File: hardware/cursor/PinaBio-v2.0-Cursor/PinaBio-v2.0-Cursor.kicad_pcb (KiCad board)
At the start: 4 copper layers, 81.3 x 57.2 mm, 80 parts, among them J1 USB-C, J2 J_BATT, J3 J_ECG, J4 J_PPG, J5 J_TEMP, J6 J_GSR, J7 J_RESP_T, J8 J_RESP_A, Q1 BSS84, Q2 BSS138, Q3 BSS138, SW1 SW_DPDT, SW2 BOOT, U1 USBLC6-2SC6, U2 BQ24074, U3 TPS63070, U4 TLV75530PDBVR, U5 ESP32-S3-MINI-1U-N8, U6 ADS122C04, U7 ADS122C04, U8 MCP6004

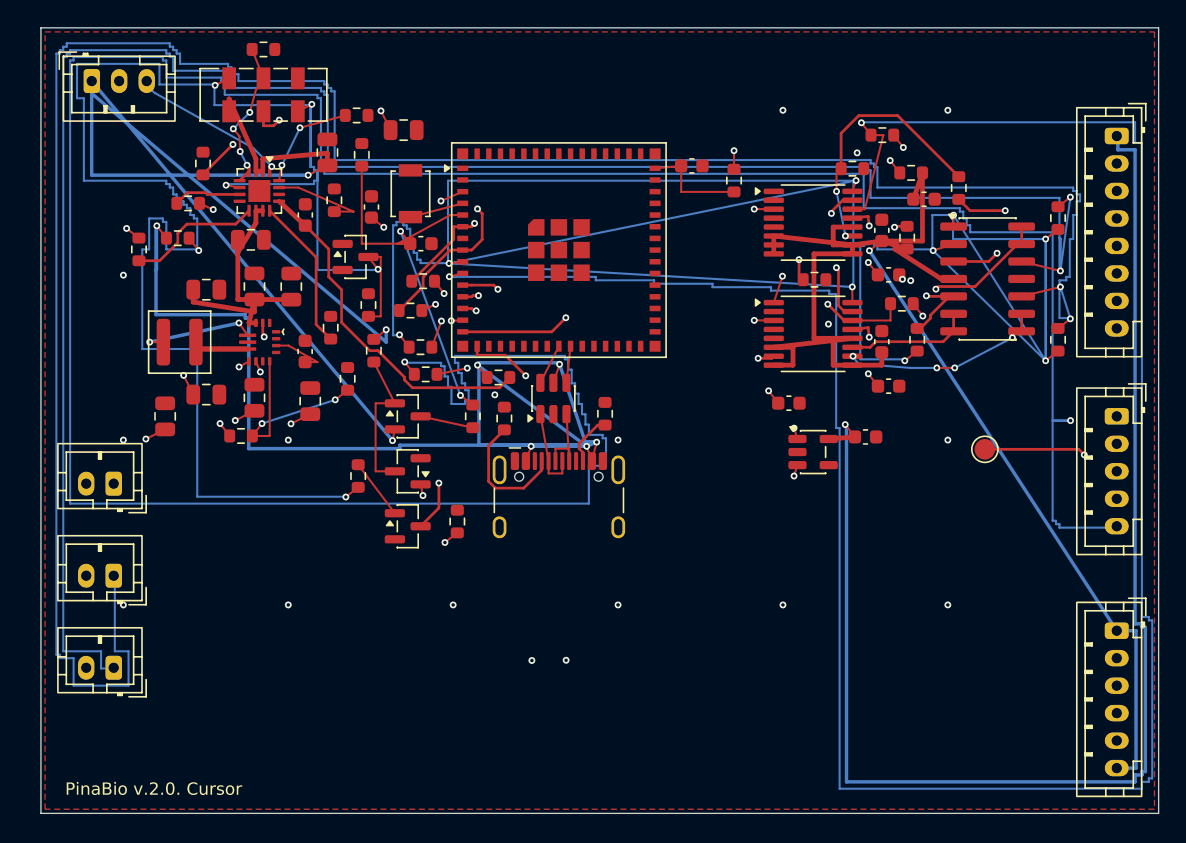
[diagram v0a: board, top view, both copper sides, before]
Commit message: Update the Cursor KiCad board to SPEC-0.9
Place the ESP32-S3-MINI-1U U.FL end on the board edge with a copper
keepout, split digital and analogue ground through one wide net tie, and
keep the six electrical changes. ERC and DRC are clean and the fab outputs
are regenerated.
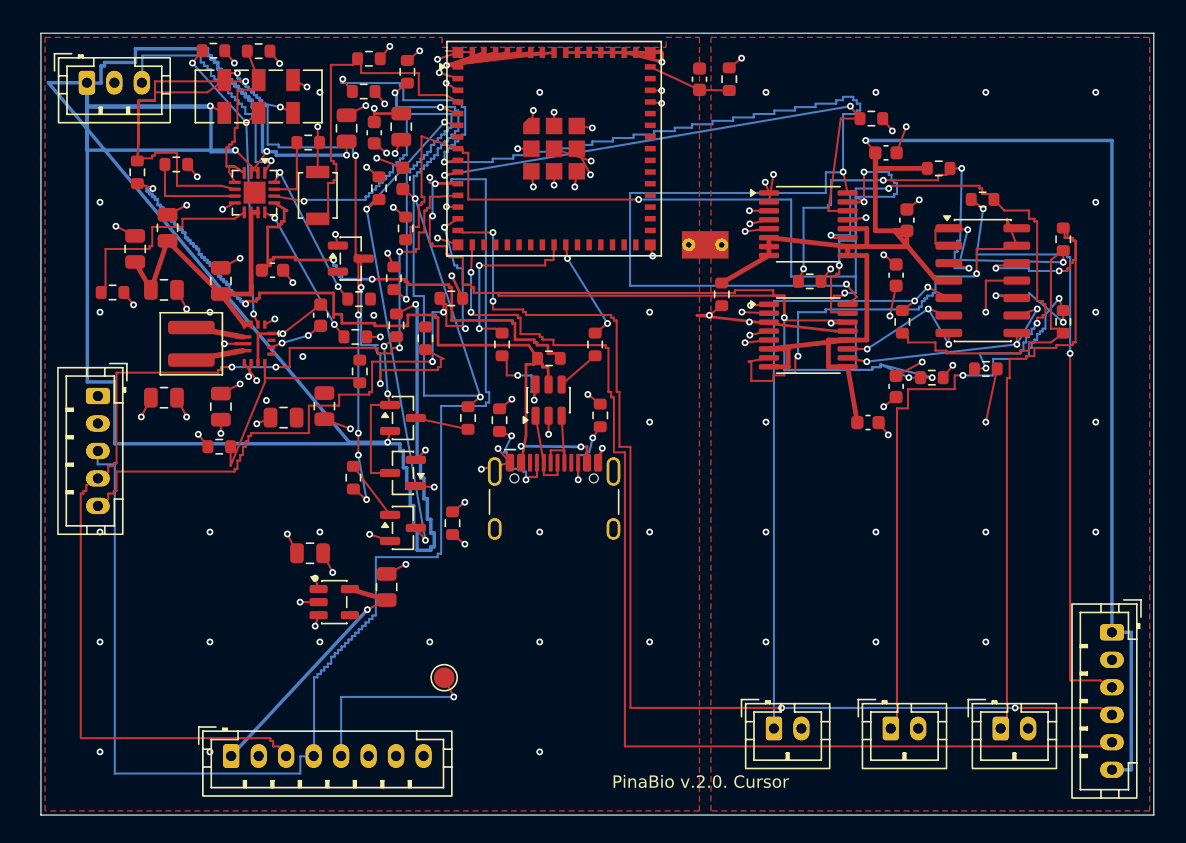
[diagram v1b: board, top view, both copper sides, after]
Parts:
- added NT1: GND_TIE, GndTie_2mm, F.Cu at (48.3, 15.8)
- added R35: 22, R_0603_1608Metric, F.Cu at (33.6, 23.0)
- added R36: 22, R_0603_1608Metric, F.Cu at (40.3, 23.0)
- added R37: 46.4k 1%, R_0603_1608Metric, F.Cu at (25.7, 18.2)
- added R38: 10k, R_0603_1608Metric, F.Cu at (23.9, 2.25)
- C12, C13: footprint C_0603_1608Metric -> C_0805_2012Metric
- moved J5 78.7 mm to (13.8, 53.0), turned to 0 degrees
- moved J4 74.2 mm to (4.14, 26.8)
- moved J8 64.7 mm to (69.8, 51.0), turned to 0 degrees
- moved J7 57.6 mm to (61.8, 51.0), turned to 0 degrees
- moved J6 51.2 mm to (53.3, 51.0), turned to 0 degrees
- moved TP1 42.7 mm to (29.3, 47.3)
- moved U4 36.5 mm to (21.3, 41.8)
- moved C13 36.5 mm to (25.2, 40.7), turned to 90 degrees
- moved C12 36.5 mm to (19.6, 38.2)
- moved R24 19.1 mm to (23.5, 4.63)
- moved R34 17.5 mm to (68.8, 24.8)
- moved R15 16.4 mm to (49.5, 19.4), turned to 90 degrees
- moved R6 13.4 mm to (23.2, 19.7)
- moved C5 9.27 mm to (8.95, 19.1), turned to 0 degrees
- moved R12 8.25 mm to (12.6, 1.66), turned to 0 degrees
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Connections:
- C18 pad 2: /GND -> /AGND
- C19 pad 2: /GND -> /AGND
- C20 pad 2: /GND -> /AGND
- C21 pad 2: /GND -> /AGND
- C22 pad 2: /GND -> /AGND
- J3 pad 2: /GND -> /AGND
- J6 pad 2: /GND -> /AGND
- J7 pad 2: /GND -> /AGND
- J8 pad 2: /GND -> /AGND
- R29 pad 2: /GND -> /AGND
- R34 pad 2: /GND -> /AGND
- U2 pad 14: (no net) -> /TMR
- U5 pad 23: /USB_DM -> /USB_DM_IO
- U5 pad 24: /USB_DP -> /USB_DP_IO
- U6 pad 1: /GND -> /AGND
- U6 pad 2: /GND -> /AGND
- U6 pad 4: /GND -> /AGND
- U6 pad 5: /GND -> /AGND
- U7 pad 2: /GND -> /AGND
- U7 pad 4: /GND -> /AGND
- U7 pad 5: /GND -> /AGND
- U8 pad 11: /GND -> /AGND
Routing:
- net /PPG_INT: track 233.4 -> 53.3 mm, vias 3 -> 4
- net /GND: track 0.00 -> 152.8 mm, vias 16 -> 75
- net /DRDY_ECG: track 168.2 -> 41.7 mm
- net /SNS_TH: track 164.4 -> 51.8 mm, vias 2 -> 4
- net /SNS_AB: track 149.6 -> 54.0 mm
- net /BAT_PROT: track 103.7 -> 198.2 mm, vias 3 -> 6
- net /3V0_TEMP: track 100.4 -> 18.9 mm
- net /DRDY_SLOW: track 33.4 -> 99.2 mm, vias 2 -> 7
- net /VLOG: track 157.4 -> 101.7 mm, vias 6 -> 10
- net /0V5_EXC: track 87.7 -> 36.2 mm, vias 5 -> 2
- net /SDA_ADC: track 47.2 -> 85.2 mm, vias 3 -> 5
- net /VBUS: track 99.9 -> 62.4 mm, vias 6 -> 4
- net /TMR: track 0.00 -> 37.1 mm, vias 0 -> 2
- net /AGND: track 0.00 -> 28.4 mm, vias 0 -> 30
- net /BAT_SENSE: track 30.3 -> 58.7 mm, vias 2 -> 4
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- added copper zone on F.Cu, net /AGND
- added copper zone on In1.Cu, net /AGND
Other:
- board size 81.3 x 57.2 mm -> 81 x 56.9 mm

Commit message: Add connector labels, the PINA logo and the Paca name on the Cursor board silk.
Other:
- board text added: "3V0"
- board text added: "3V3"
- board text added: "AB"
- board text added: "AGND"
- board text added: "BAT+"
- board text added: "BATERIA"
- board text added: "CC1"
- board text added: "CC2"
- board text added: "D+"
- board text added: "D-"
- board text added: "ECG"
- board text added: "GND"
- board text added: "GSR"
- board text added: "INT"
- board text added: "LO+"
- board text added: "LO-"
- board text added: "OS"
- board text added: "OUT"
- board text added: "PPG"
- board text added: "PinaBio "Paca" v2.0"
- board text added: "RESP A"
- board text added: "RESP T"
- board text added: "SBU"
- board text added: "SCL"
- board text added: "SDA"
- board text added: "TEMP"
- board text added: "TH"
- board text added: "TS"
- board text added: "USB"
- board text added: "VBUS"
- board text removed: "PinaBio v.2.0. Cursor"

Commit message: Fix mirrored TPS63070 footprint (TI 4222000/B), reroute the TPS63070 zone, portable library tables
U3 pin 1 is now top left with counter-clockwise numbering, pads 9-11 use the TI sizes, L1 sits east of U3 with both switch nodes on F.Cu without vias. fp-lib-table and sym-lib-table use KIPRJMOD and KICAD9_SYMBOL_DIR. ERC, DRC, fab, position, netlist and render regenerated.
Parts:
- moved R14 11.1 mm to (12.1, 24.9), turned to 180 degrees
- moved L1 8.86 mm to (19.8, 23.3)
- moved C11 8.58 mm to (12.1, 23.2), turned to 180 degrees
- moved R8 8.03 mm to (18.3, 15.9)
- moved R13 3.94 mm to (15.0, 27.1), turned to 90 degrees
- turned U3 to 0 degrees
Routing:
- net /FB: track 17.5 -> 2.54 mm
- net /ILIM: track 10.9 -> 2.14 mm
- net /GND: track 152.8 -> 147.4 mm, vias 75 -> 84
- net /VAUX: track 3.96 -> 0.80 mm, vias 2 -> 0
- net /3V3_SYS: track 52.4 -> 50.9 mm
- net /SW_L1: track 3.81 -> 2.30 mm
- net /SW_L2: track 3.81 -> 2.43 mm
- net /SDA_MOD: track 82.8 -> 82.2 mm
- net /TPS_EN: track 22.9 -> 22.4 mm
- net /SYS: track 23.5 -> 23.4 mm, vias 0 -> 2

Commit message: J5 (J_TEMP) pasa a 4 pines: 3V0_TEMP, GND, SDA_MOD, SCL_MOD; se quitan OS y TP1
JST PH B4B-PH-K en esquema, PCB, BOM, position.csv y pinabio.net. A0, A1 y A2 del CJMCU-30205 van a GND en el modulo; OS queda sin conectar. Gerbers, pcb-top.png, ERC y DRC regenerados; spec ES/EN y README actualizados.
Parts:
- removed TP1: OS, TestPoint_Pad_D1.5mm
- J5: footprint JST_PH_B8B-PH-K_1x08_P2.00mm_Vertical -> JST_PH_B4B-PH-K_1x04_P2.00mm_Vertical
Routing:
- net /OS: track 14.1 -> 0.00 mm, vias 1 -> 0
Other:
- board text removed: "OS"

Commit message: Add purchasable BOM fields and schematic-PCB parity
Symbols and bom.csv now carry manufacturer and MPN, and capacitors
carry voltage and dielectric. Footprints keep the library nickname and
unconnected pads use the schematic net name. Electrical values, tracks
and copper are unchanged.
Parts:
- C1, C11, C14, C15, C17, C18, C19, C20, C21, C22: footprint C_0603_1608Metric -> Capacitor_SMD:C_0603_1608Metric
- C10, C12, C13, C16, C2, C3, C4, C5, C6, C7, C8, C9: footprint C_0805_2012Metric -> Capacitor_SMD:C_0805_2012Metric
- D1, Q1, Q2, Q3: footprint SOT-23 -> Package_TO_SOT_SMD:SOT-23
- J1: footprint USB_C_Receptacle_HCTL_HC-TYPE-C-16P-01A -> Connector_USB:USB_C_Receptacle_HCTL_HC-TYPE-C-16P-01A
- J2: footprint JST_PH_B3B-PH-K_1x03_P2.00mm_Vertical -> Connector_JST:JST_PH_B3B-PH-K_1x03_P2.00mm_Vertical
- J3: footprint JST_PH_B6B-PH-K_1x06_P2.00mm_Vertical -> Connector_JST:JST_PH_B6B-PH-K_1x06_P2.00mm_Vertical
- J4: footprint JST_PH_B5B-PH-K_1x05_P2.00mm_Vertical -> Connector_JST:JST_PH_B5B-PH-K_1x05_P2.00mm_Vertical
- J5: footprint JST_PH_B4B-PH-K_1x04_P2.00mm_Vertical -> Connector_JST:JST_PH_B4B-PH-K_1x04_P2.00mm_Vertical
- J6, J7, J8: footprint JST_PH_B2B-PH-K_1x02_P2.00mm_Vertical -> Connector_JST:JST_PH_B2B-PH-K_1x02_P2.00mm_Vertical
- L1: footprint L_Coilcraft_XAL4020-XXX -> Inductor_SMD:L_Coilcraft_XAL4020-XXX
- NT1: footprint GndTie_2mm -> PinaCursor:GndTie_2mm
- R1, R10, R11, R12, R13, R14, R15, R16, R17, R18, R19, R2, R20, R21, R22, R23, R24, R25, R26, R27, R28, R29, R3, R30, R31, R32, R33, R34, R35, R36, R37, R38, R4, R5, R6, R7, R8, R9: footprint R_0603_1608Metric -> Resistor_SMD:R_0603_1608Metric
- SW1: footprint SW_DPDT_CK_JS202011JCQN -> Button_Switch_SMD:SW_DPDT_CK_JS202011JCQN
- SW2: footprint SW_SPST_B3U-1000P -> Button_Switch_SMD:SW_SPST_B3U-1000P
- U1: footprint SOT-23-6 -> Package_TO_SOT_SMD:SOT-23-6
- U2: footprint VQFN-16-1EP_3x3mm_P0.5mm_EP1.6x1.6mm -> Package_DFN_QFN:VQFN-16-1EP_3x3mm_P0.5mm_EP1.6x1.6mm
- U3: footprint TPS63070RNM -> PinaCursor:TPS63070RNM
- U4: footprint SOT-23-5 -> Package_TO_SOT_SMD:SOT-23-5
- U5: footprint ESP32-S2-MINI-1U -> RF_Module:ESP32-S2-MINI-1U
- U6, U7: footprint TSSOP-16_4.4x5mm_P0.65mm -> Package_SO:TSSOP-16_4.4x5mm_P0.65mm
- U8: footprint SOIC-14_3.9x8.7mm_P1.27mm -> Package_SO:SOIC-14_3.9x8.7mm_P1.27mm
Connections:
- D1 pad 2: (no net) -> unconnected-(D1-NC-Pad2)
- J1 pad A8: (no net) -> unconnected-(J1-SBU1-PadA8)
- J1 pad B8: (no net) -> unconnected-(J1-SBU2-PadB8)
- U3 pad 2: (no net) -> unconnected-(U3-PG-Pad2)
- U4 pad 4: (no net) -> unconnected-(U4-NC-Pad4)
- U5 pad 17: (no net) -> unconnected-(U5-IO13-Pad17)
- U5 pad 18: (no net) -> unconnected-(U5-IO14-Pad18)
- U5 pad 19: (no net) -> unconnected-(U5-IO15-Pad19)
- U5 pad 20: (no net) -> unconnected-(U5-IO16-Pad20)
- U5 pad 21: (no net) -> unconnected-(U5-IO17-Pad21)
- U5 pad 22: (no net) -> unconnected-(U5-IO18-Pad22)
- U5 pad 25: (no net) -> unconnected-(U5-IO21-Pad25)
- U5 pad 26: (no net) -> unconnected-(U5-IO26-Pad26)
- U5 pad 27: (no net) -> unconnected-(U5-IO47-Pad27)
- U5 pad 28: (no net) -> unconnected-(U5-IO33-Pad28)
- U5 pad 29: (no net) -> unconnected-(U5-IO34-Pad29)
- U5 pad 30: (no net) -> unconnected-(U5-IO48-Pad30)
- U5 pad 31: (no net) -> unconnected-(U5-IO35-Pad31)
- U5 pad 32: (no net) -> unconnected-(U5-IO36-Pad32)
- U5 pad 33: (no net) -> unconnected-(U5-IO37-Pad33)
- U5 pad 34: (no net) -> unconnected-(U5-IO38-Pad34)
- U5 pad 35: (no net) -> unconnected-(U5-IO39-Pad35)
- U5 pad 36: (no net) -> unconnected-(U5-IO40-Pad36)
- U5 pad 37: (no net) -> unconnected-(U5-IO41-Pad37)
- U5 pad 38: (no net) -> unconnected-(U5-IO42-Pad38)
- U5 pad 39: (no net) -> unconnected-(U5-TXD0-Pad39)
- U5 pad 40: (no net) -> unconnected-(U5-RXD0-Pad40)
- U5 pad 41: (no net) -> unconnected-(U5-IO45-Pad41)
- U5 pad 44: (no net) -> unconnected-(U5-IO46-Pad44)
- U5 pad 7: (no net) -> unconnected-(U5-IO3-Pad7)

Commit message: Dejar el DPDT en la caja y fijar la bobina XAL4020
Seis taladros conservan las redes del interruptor, con ON, OFF y COM en la serigrafía. La pieza de caja es el C&K 7201SYZQE. L1 queda como Coilcraft XAL4020-152ME. La masa del TPS63070 no se mueve.
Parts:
- SW1: value SW_DPDT -> DPDT caja; footprint Button_Switch_SMD:SW_DPDT_CK_JS202011JCQN -> PinaCursor:SW_ext_6pad
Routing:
- net /BAT_PROT: track 198.2 -> 189.0 mm, vias 6 -> 5
- net /VLOG: track 101.7 -> 96.6 mm, vias 10 -> 11
- net /TPS_EN: track 22.4 -> 24.9 mm
- net /TS: track 20.3 -> 19.5 mm
